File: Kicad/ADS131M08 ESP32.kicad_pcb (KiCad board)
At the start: 2 copper layers, 85 x 50 mm, 85 parts, among them J1 Conn_01x02, J2 Conn_02x10_Odd_Even, SW1 SW_SPDT, SW2 SW_Push, SW3 SW_Push, U1 LIS3DH, U2 ESP32-DevKitC, U3 ADS131M08, U4 LP5907MFX-3.3, X1 SIT8924BA

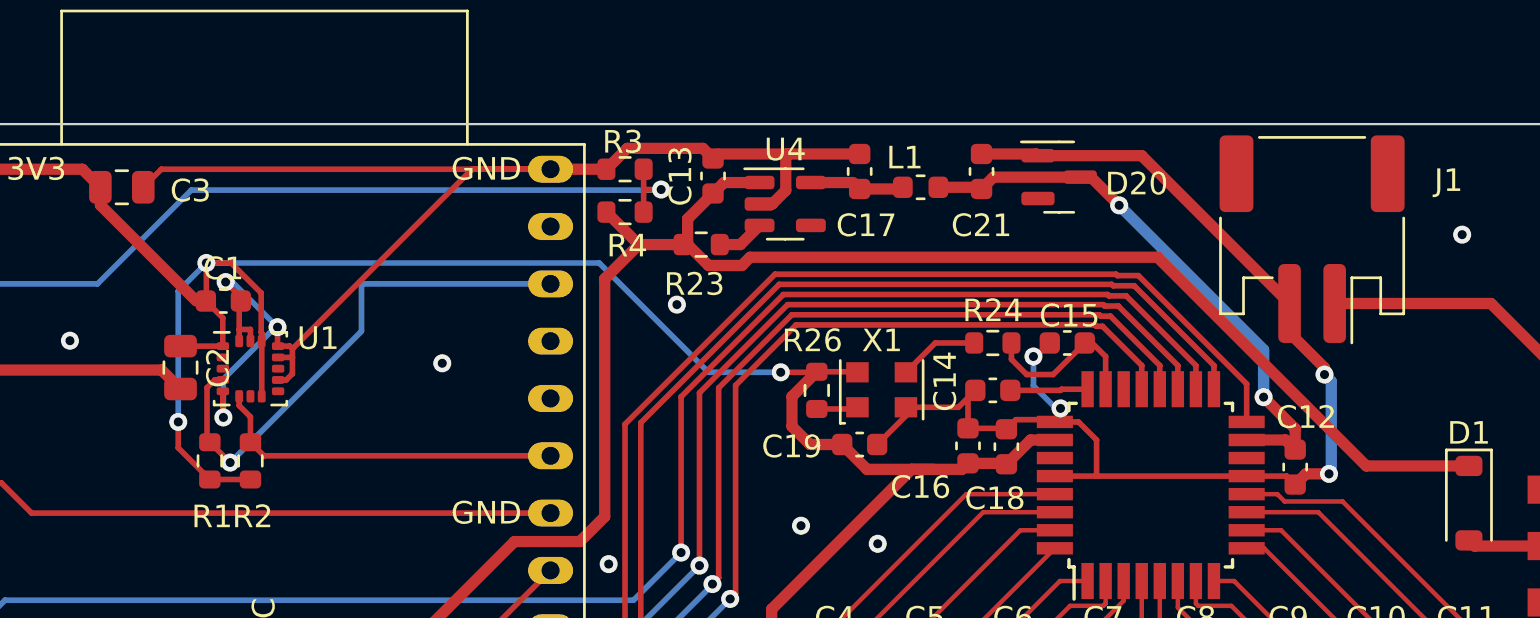
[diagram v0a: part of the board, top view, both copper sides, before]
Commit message: Update ADS131M08 ESP32.kicad_pcb
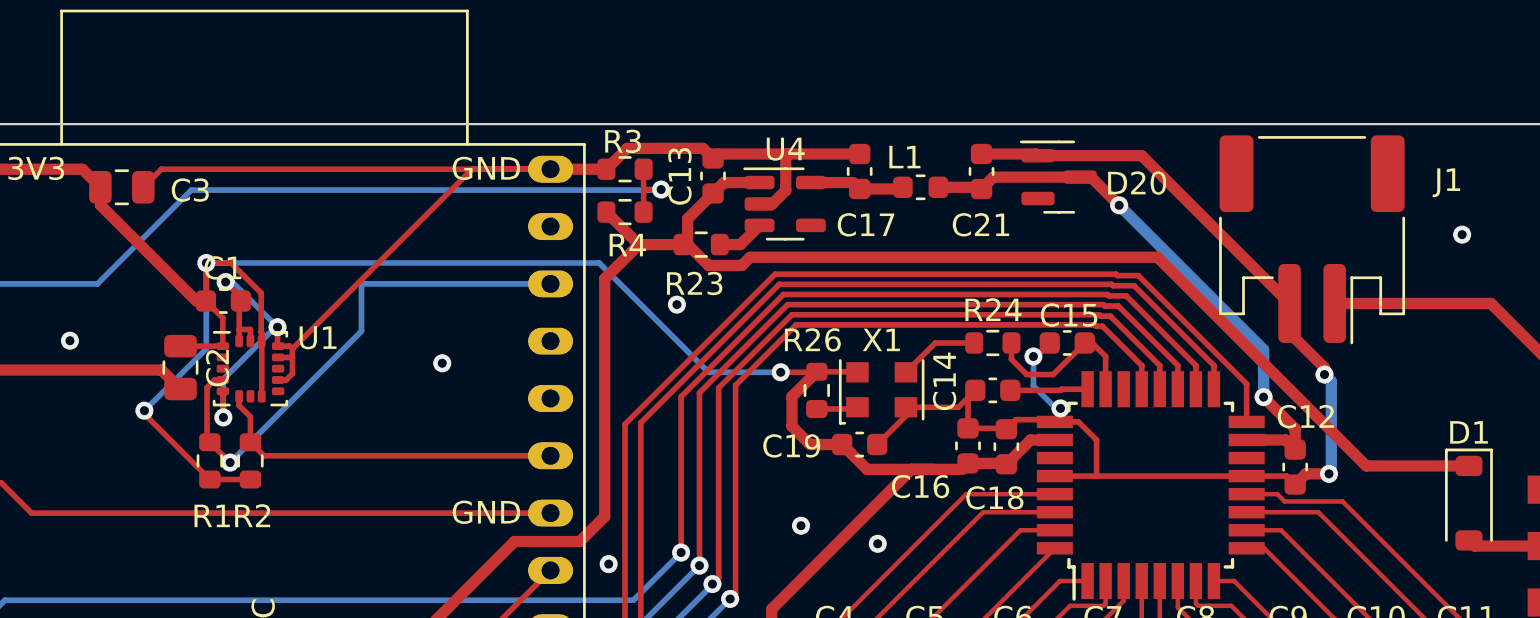
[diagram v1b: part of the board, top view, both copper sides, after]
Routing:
- net +3.3V: track 116.9 -> 118.2 mm
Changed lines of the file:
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@@
       (outputformat 1)
       (mirror false)
-      (drillshape 1)
+      (drillshape 0)
       (scaleselection 1)
-      (outputdirectory "")
+      (outputdirectory "Gerbers/")
     )
   )
@@
     (pad "2" smd roundrect (at 1 -2.85 180) (size 1 3.5) (layers "F.Cu" "F.Paste" "F.Mask") (roundrect_rratio 0.25)
       (net 2 "GND") (pinfunction "Pin_2") (pintype "passive"))
-    (pad "MP" smd roundrect (at -3.35 2.9 180) (size 1.5 3.4) (layers "F.Cu" "F.Paste" "F.Mask") (roundrect_rratio 0.166667))
-    (pad "MP" smd roundrect (at 3.35 2.9 180) (size 1.5 3.4) (layers "F.Cu" "F.Paste" "F.Mask") (roundrect_rratio 0.166667))
+    (pad "MP" smd roundrect (at -3.35 2.9 180) (size 1.5 3.4) (layers "F.Cu" "F.Paste" "F.Mask") (roundrect_rratio 0.1666673333))
+    (pad "MP" smd roundrect (at 3.35 2.9 180) (size 1.5 3.4) (layers "F.Cu" "F.Paste" "F.Mask") (roundrect_rratio 0.1666673333))
     (model "${KICAD6_3DMODEL_DIR}/Connector_JST.3dshapes/JST_PH_S2B-PH-SM4-TB_1x02-1MP_P2.00mm_Horizontal.wrl"
       (offset (xyz 0 0 0))
@@
   (segment (start 159.7875 85.6625) (end 156.425 82.3) (width 0.5) (layer "F.Cu") (net 1))
   (segment (start 160.2 76.625) (end 160.2 71.5) (width 0.5) (layer "F.Cu") (net 1))
+  (segment (start 135.3 65.75) (end 132.4 62.85) (width 0.25) (layer "F.Cu") (net 1))
   (segment (start 156.425 80.4) (end 160.2 76.625) (width 0.5) (layer "F.Cu") (net 1))
   (segment (start 172.75 64) (end 171.675 64) (width 0.5) (layer "F.Cu") (net 1))
@@
   (segment (start 135.875 58.59) (end 135.125 57.84) (width 0.25) (layer "F.Cu") (net 1))
   (segment (start 161.1 63.4) (end 161.1 62.075) (width 0.5) (layer "F.Cu") (net 1))
+  (segment (start 132.4 62.85) (end 132.4 62.7) (width 0.25) (layer "F.Cu") (net 1))
   (segment (start 159.7875 87) (end 159.7875 85.6625) (width 0.5) (layer "F.Cu") (net 1))
   (segment (start 137.6 62.065) (end 137.6 59.615) (width 0.25) (layer "F.Cu") (net 1))
@@
   (segment (start 162.2 60.975) (end 163.975 60.975) (width 0.25) (layer "F.Cu") (net 1))
   (segment (start 130.45 53.59) (end 130.45 52.8) (width 0.5) (layer "F.Cu") (net 1))
-  (segment (start 133.9 64.35) (end 133.9 63.2) (width 0.25) (layer "F.Cu") (net 1))
   (segment (start 168.635 65.3) (end 168.9 65.035) (width 0.5) (layer "F.Cu") (net 1))
   (segment (start 171.675 64) (end 170.6 65.075) (width 0.5) (layer "F.Cu") (net 1))
@@
   (segment (start 135.145 57.82) (end 135.125 57.84) (width 0.25) (layer "F.Cu") (net 1))
   (segment (start 129.65 52) (end 125 52) (width 0.5) (layer "F.Cu") (net 1))
-  (segment (start 135.3 65.75) (end 133.9 64.35) (width 0.25) (layer "F.Cu") (net 1))
   (segment (start 161.9 64.2) (end 161.1 63.4) (width 0.5) (layer "F.Cu") (net 1))
   (segment (start 163.975 60.975) (end 164 61) (width 0.25) (layer "F.Cu") (net 1))
@@
   (segment (start 166.4 65.3) (end 167.4 65.3) (width 0.5) (layer "F.Cu") (net 1))
   (via (at 135.145 56.155) (size 0.8) (drill 0.4) (layers "F.Cu" "B.Cu") (net 1))
-  (via (at 133.9 63.2) (size 0.8) (drill 0.4) (layers "F.Cu" "B.Cu") (net 1))
+  (via (at 132.4 62.7) (size 0.8) (drill 0.4) (layers "F.Cu" "B.Cu") (net 1))
   (via (at 160.6 61) (size 0.8) (drill 0.4) (layers "F.Cu" "B.Cu") (net 1))
+  (segment (start 135.145 56.155) (end 135.145 59.955) (width 0.25) (layer "B.Cu") (net 1))
   (segment (start 152.555 56.155) (end 135.145 56.155) (width 0.25) (layer "B.Cu") (net 1))
   (segment (start 157.4 61) (end 152.555 56.155) (width 0.25) (layer "B.Cu") (net 1))
   (segment (start 160.6 61) (end 157.4 61) (width 0.25) (layer "B.Cu") (net 1))
-  (segment (start 133.9 63.2) (end 133.9 57.4) (width 0.25) (layer "B.Cu") (net 1))
-  (segment (start 133.9 57.4) (end 135.145 56.155) (width 0.25) (layer "B.Cu") (net 1))
+  (segment (start 135.145 59.955) (end 132.4 62.7) (width 0.25) (layer "B.Cu") (net 1))
   (segment (start 132.35 52.8) (end 133.15 52) (width 0.25) (layer "F.Cu") (net 2))
   (segment (start 188.925 86.69) (end 188.925 89.23) (width 0.25) (layer "F.Cu") (net 2))

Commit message: Fix PCB Issues
Fix ADS131M08 Pinout
Fix ADS131M08 footprint size
Replace tiny ESD devices
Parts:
- removed D10, D11, D12, D13, D14, D15, D16, D17, D18, D19, D8, D9: PESD2V0Y1, Diode_SMD:D_SOD-923
- D4, D5, D6, D7: value PESD2V0Y1 -> ESDA6V1BC6; footprint Diode_SMD:D_SOD-923 -> Package_TO_SOT_SMD:SOT-23-6
- U3: footprint Package_QFP:TQFP-32_7x7mm_P0.8mm -> Package_QFP:PQFP-32_5x5mm_P0.5mm
- moved D4 27.0 mm to (165.0, 82.0)
- moved D5 15.0 mm to (173.0, 82.0)
- moved D7 9.05 mm to (189.0, 82.0)
- moved D6 3.16 mm to (181.0, 82.0)
- moved C14 3.14 mm to (173.1, 62.1)
- moved C16 2.29 mm to (170.8, 65.5), turned to 180 degrees
- moved R10 2.00 mm to (166.0, 75.5)
- moved R13 2.00 mm to (176.0, 75.5)
- moved R14 2.00 mm to (174.0, 75.5)
- moved R17 2.00 mm to (184.0, 75.5)
- moved R18 2.00 mm to (182.0, 75.5)
- moved R21 2.00 mm to (192.0, 75.5)
- moved R22 2.00 mm to (190.0, 75.5)
- moved R9 2.00 mm to (168.0, 75.5)
- moved C12 1.41 mm to (182.3, 64.3)
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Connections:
- D4 pad 1: /ADS131M08_Input/IN7N -> /ADS131M08_Input/IN0P
- D5 pad 1: /ADS131M08_Input/IN6N -> /ADS131M08_Input/IN2P
- D6 pad 1: /ADS131M08_Input/IN5N -> /ADS131M08_Input/IN4P
- D7 pad 1: /ADS131M08_Input/IN4N -> /ADS131M08_Input/IN6P
- U3 pad 11: /ADS131M08_Input/AIN7P -> /ADS131M08_Input/AIN7N
- U3 pad 12: /ADS131M08_Input/AIN7N -> /ADS131M08_Input/AIN7P
- U3 pad 3: /ADS131M08_Input/AIN3P -> /ADS131M08_Input/AIN3N
- U3 pad 31: /ADS131M08_Input/AIN1P -> /ADS131M08_Input/AIN1N
- U3 pad 32: /ADS131M08_Input/AIN1N -> /ADS131M08_Input/AIN1P
- U3 pad 4: /ADS131M08_Input/AIN3N -> /ADS131M08_Input/AIN3P
- U3 pad 7: /ADS131M08_Input/AIN5P -> /ADS131M08_Input/AIN5N
- U3 pad 8: /ADS131M08_Input/AIN5N -> /ADS131M08_Input/AIN5P
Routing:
- net GND: track 217.4 -> 195.1 mm, vias 39 -> 24
- net +3.3V: track 118.2 -> 123.8 mm, vias 3 -> 4
- net /ADS131M08_Input/AIN1N: track 8.48 -> 11.7 mm
- net /ADS131M08_Input/AIN7P: track 13.1 -> 16.1 mm
- net /ADS131M08_Input/AIN5P: track 6.72 -> 8.98 mm
- net /ADS131M08_Input/AIN2P: track 6.88 -> 8.80 mm
- net /ADS131M08_Input/IN4N: track 13.8 -> 15.5 mm, vias 0 -> 1
- net /ADS131M08_Input/IN6P: track 11.6 -> 13.3 mm
- net /ADS131M08_Input/AIN6P: track 8.48 -> 10.1 mm
- net /ADS131M08_Input/AIN3N: track 4.86 -> 6.41 mm
- net /ADS131M08_Input/IN1P: track 12.8 -> 14.3 mm
- net /ADS131M08_Input/IN7P: track 12.2 -> 13.7 mm
- net /ADS131M08_Input/AIN6N: track 10.4 -> 11.7 mm
- net /ADS131M08_Input/AIN0N: track 13.1 -> 14.4 mm
- net /ADS131M08_Input/AIN4N: track 5.17 -> 6.41 mm
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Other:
- board text added: "ADS131M08 EMG Input Board Rev 2.0"
- board text removed: "ADS131M08 EMG Input Board"
